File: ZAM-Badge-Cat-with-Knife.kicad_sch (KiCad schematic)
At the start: 4 parts, among them SW101 SW_SPDT

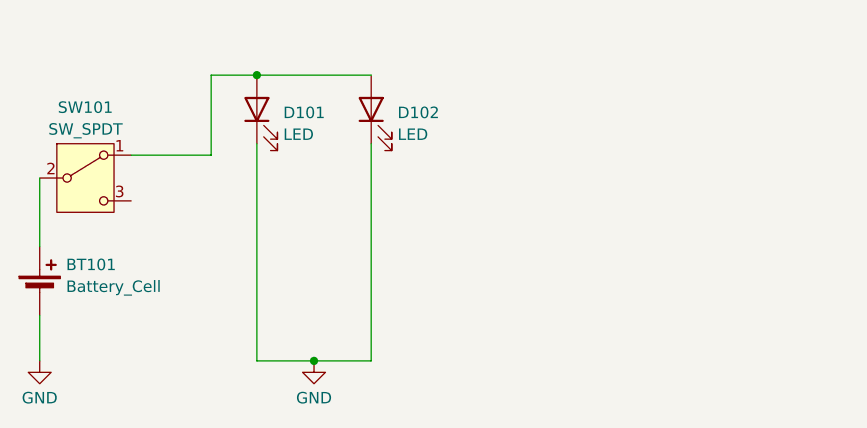
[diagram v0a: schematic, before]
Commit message: Finalise the layout and add ZAM logo and a placeholder for the butterfly pin
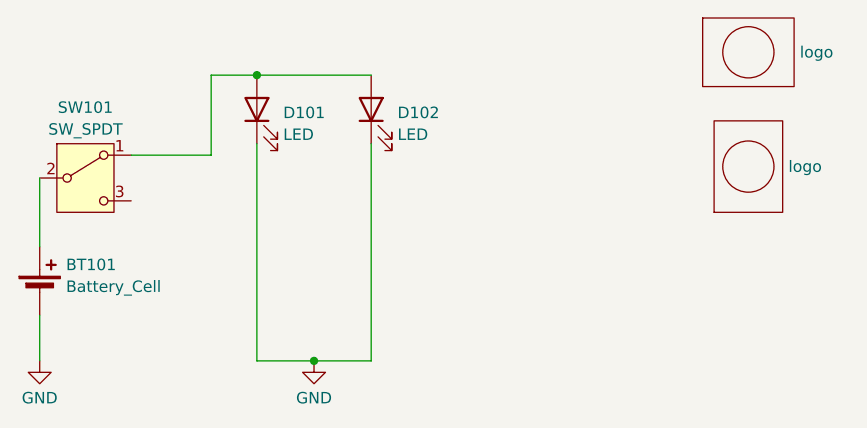
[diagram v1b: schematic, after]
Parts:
- added Lg101: logo, Cat-with-Knife:ZAM_LOGO_440, symbol sjm-mechanical:logo
- added Lg102: logo, Cat-with-Knife:Butterfy-Pin, symbol mech:logo
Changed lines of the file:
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@@
+	)
+	(symbol
+		(lib_id "sjm-mechanical:logo")
+		(at 195.58 46.99 0)
+		(unit 1)
+		(exclude_from_sim no)
+		(in_bom yes)
+		(on_board yes)
+		(dnp no)
+		(fields_autoplaced yes)
+		(property "Reference" "Lg101"
+			(at 195.58 46.99 0)
+			(effects
+				(font
+					(size 1.27 1.27)
+				)
+				(hide yes)
+			)
+		)
+		(property "Value" "logo"
+			(at 201.295 46.99 0)
+			(effects
+				(font
+					(size 1.27 1.27)
+				)
+				(justify left)
+			)
+		)
+		(property "Footprint" "Cat-with-Knife:ZAM_LOGO_440"
+			(at 195.58 46.99 0)
+			(effects
+				(font
+					(size 1.27 1.27)
+				)
+				(hide yes)
+			)
+		)
+		(property "Datasheet" ""
+			(at 195.58 46.99 0)
+			(effects
+				(font
+					(size 1.27 1.27)
+				)
+				(hide yes)
+			)
+		)
+		(property "Description" ""
+			(at 195.58 46.99 0)
+			(effects
+				(font
+					(size 1.27 1.27)
+				)
+				(hide yes)
+			)
+		)
+		(instances
+			(project ""
+				(path "/ce43b50f-4dae-48ce-9c8b-2295cbb97664"
+					(reference "Lg101")
+					(unit 1)
+				)
+			)
+		)
 	)
 	(symbol
@@
 					(unit 1)
 				)
+			)
+		)
+	)
+	(symbol
+		(lib_id "mech:logo")
+		(at 195.58 59.69 90)
+		(unit 1)
+		(exclude_from_sim no)
+		(in_bom yes)
+		(on_board yes)
+		(dnp no)
+		(fields_autoplaced yes)
+		(property "Reference" "Lg102"
+			(at 195.58 59.69 0)
+			(effects
+				(font
+					(size 1.27 1.27)
+				)
+				(hide yes)
+			)
+		)
+		(property "Value" "logo"
+			(at 200.025 59.69 90)
+			(effects
+				(font
+					(size 1.27 1.27)
+				)
+				(justify right)
+			)
+		)
+		(property "Footprint" "Cat-with-Knife:Butterfy-Pin"
+			(at 195.58 59.69 0)
+			(effects
+				(font
+					(size 1.27 1.27)
+				)
+				(hide yes)
+			)
+		)
+		(property "Datasheet" ""
+			(at 195.58 59.69 0)
+			(effects
+				(font
+					(size 1.27 1.27)
+				)
+				(hide yes)
+			)
+		)
+		(property "Description" ""
+			(at 195.58 59.69 0)
+			(effects
+				(font
+					(size 1.27 1.27)
+				)
+				(hide yes)
+			)
+		)
+		(instances
+			(project ""
+				(path "/ce43b50f-4dae-48ce-9c8b-2295cbb97664"
+					(reference "Lg102")
+					(unit 1)
+				)
